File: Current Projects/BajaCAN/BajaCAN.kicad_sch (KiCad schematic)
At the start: 21 parts, among them J1 Conn_01x04, J2 ICSP, J3 Conn_01x04, U1 AVR128DB32x-xPT, U3 MCP1603, U4 MCP251863T-H-SS, Y1 OV-7604-C7, Y2 CSTNE16M0VH3C000R0

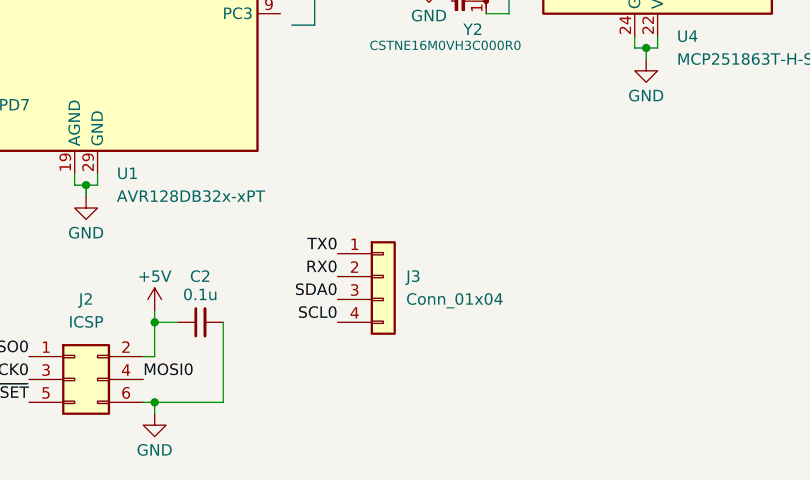
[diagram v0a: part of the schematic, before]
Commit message: Deleted extra header
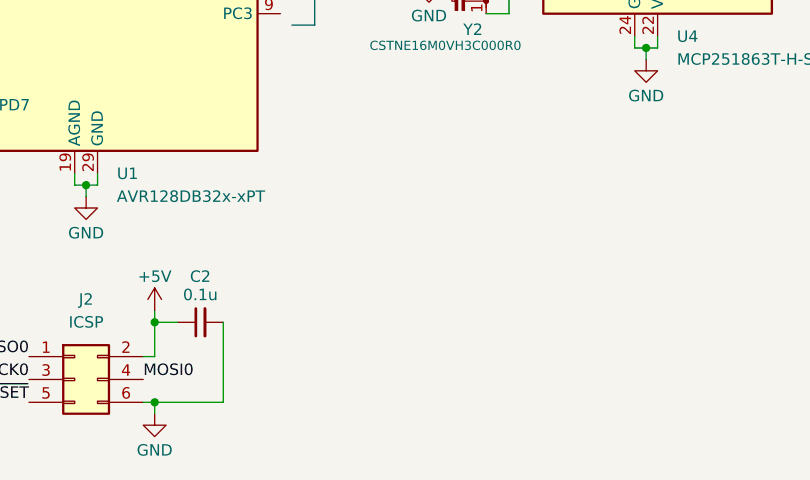
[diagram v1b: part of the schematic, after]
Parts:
- removed J3: Conn_01x04, symbol Connector_Generic:Conn_01x04
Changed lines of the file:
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@@
-	)
-	(label "RX0"
-		(at 172.72 134.62 180)
-		(effects
-			(font
-				(size 1.27 1.27)
-			)
-			(justify right bottom)
-		)
 	)
 	(label "RX0"
@@
 		)
 	)
-	(label "SCL0"
-		(at 172.72 139.7 180)
-		(effects
-			(font
-				(size 1.27 1.27)
-			)
-			(justify right bottom)
-		)
-	)
 	(label "CAN_L"
 		(at 245.11 74.93 180)
@@
 		)
 	)
-	(label "SDA0"
-		(at 172.72 137.16 180)
-		(effects
-			(font
-				(size 1.27 1.27)
-			)
-			(justify right bottom)
-		)
-	)
 	(label "SCK0"
 		(at 138.43 146.05 180)
@@
 	(label "~{RESET}"
 		(at 138.43 148.59 180)
-		(effects
-			(font
-				(size 1.27 1.27)
-			)
-			(justify right bottom)
-		)
-	)
-	(label "TX0"
-		(at 172.72 132.08 180)
 		(effects
 			(font
@@
 					(unit 1)
 				)
-			)
-		)
-	)
-	(symbol
-		(lib_id "Connector_Generic:Conn_01x04")
-		(at 177.8 134.62 0)
-		(unit 1)
-		(exclude_from_sim no)
-		(in_bom yes)
-		(on_board yes)
-		(dnp no)
-		(fields_autoplaced yes)
-		(property "Reference" "J3"
-			(at 180.34 134.6199 0)
-			(effects
-				(font
-					(size 1.27 1.27)
-				)
-				(justify left)
-			)
-		)
-		(property "Value" "Conn_01x04"
-			(at 180.34 137.1599 0)
-			(effects
-				(font
-					(size 1.27 1.27)
-				)
-				(justify left)
-			)
-		)
-		(property "Footprint" ""
-			(at 177.8 134.62 0)
-			(effects
-				(font
-					(size 1.27 1.27)
-				)
-				(hide yes)
-			)
-		)
-		(property "Datasheet" "~"
-			(at 177.8 134.62 0)
-			(effects
-				(font
-					(size 1.27 1.27)
-				)
-				(hide yes)
-			)
-		)
-		(property "Description" "Generic connector, single row, 01x04, script generated (kicad-library-utils/schlib/autogen/connector/)"
-			(at 177.8 134.62 0)
-			(effects
-				(font
-					(size 1.27 1.27)
-				)
-				(hide yes)
-			)
-		)
-		(pin "1"
-		)
-		(pin "2"
-		)
-		(pin "3"
-		)
-		(pin "4"
-		)
-		(instances
-			(project ""
-				(path "/e8fd5210-53c5-4e8b-9e8d-a6cec89a0b03"
-					(reference "J3")
-					(unit 1)
-				)

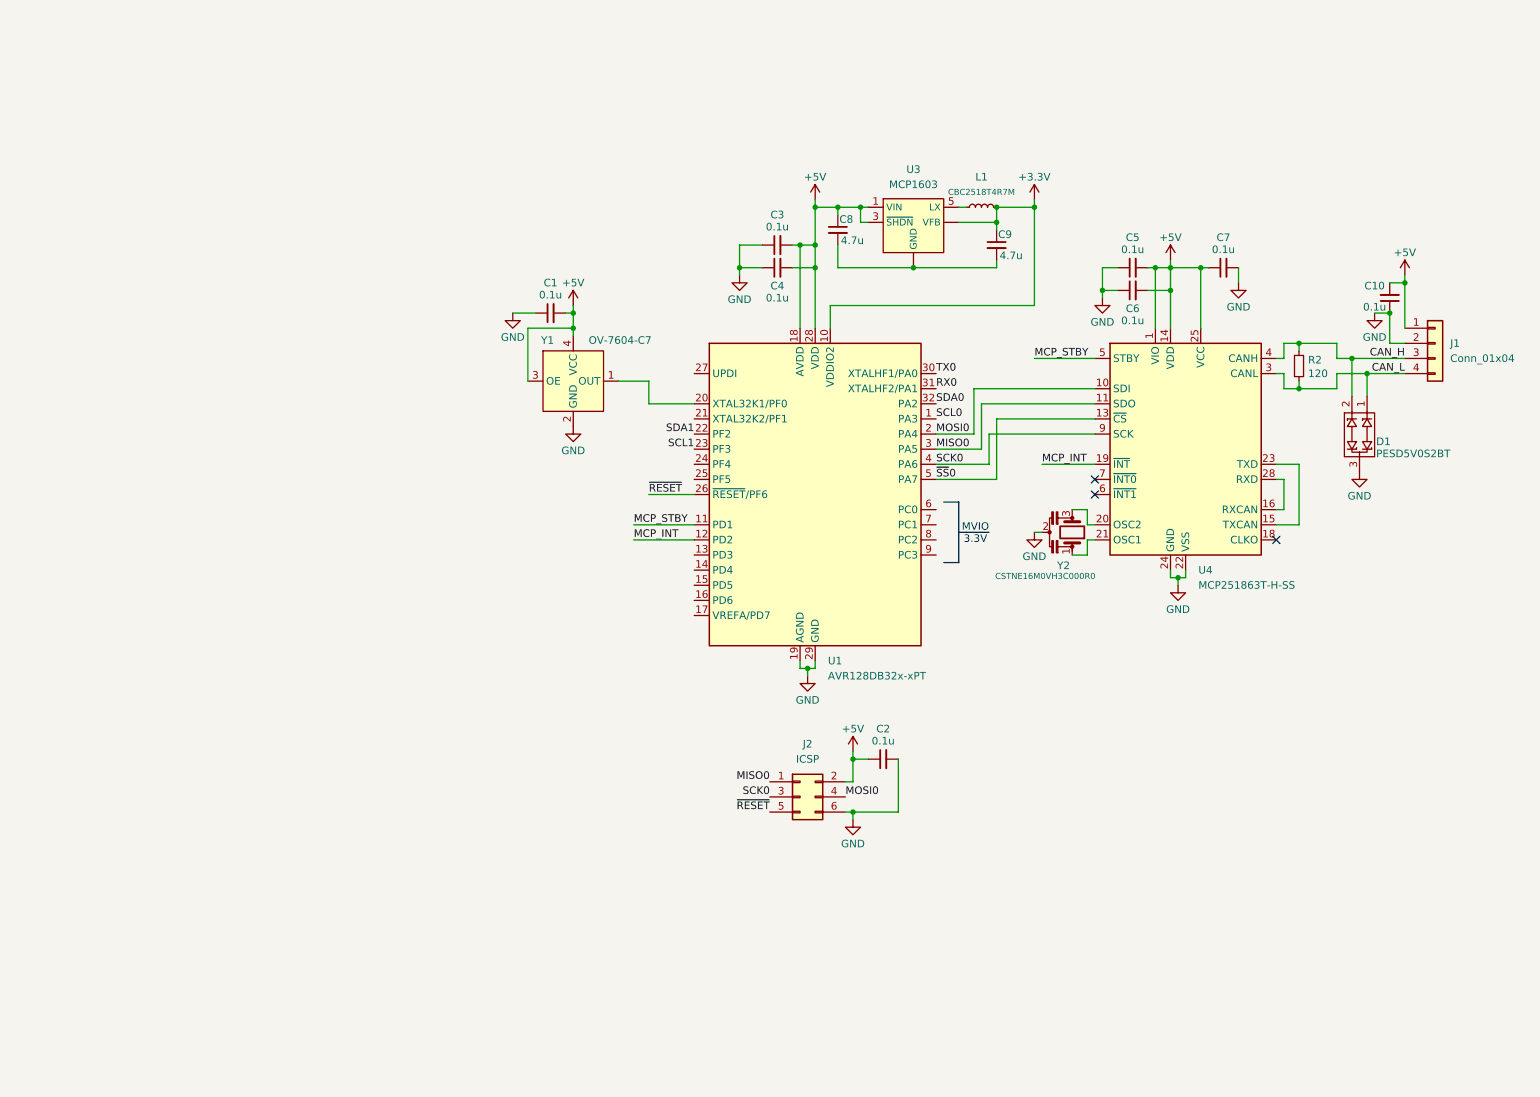
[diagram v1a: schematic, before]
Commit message: Added I/O molex conns
A and D keyed
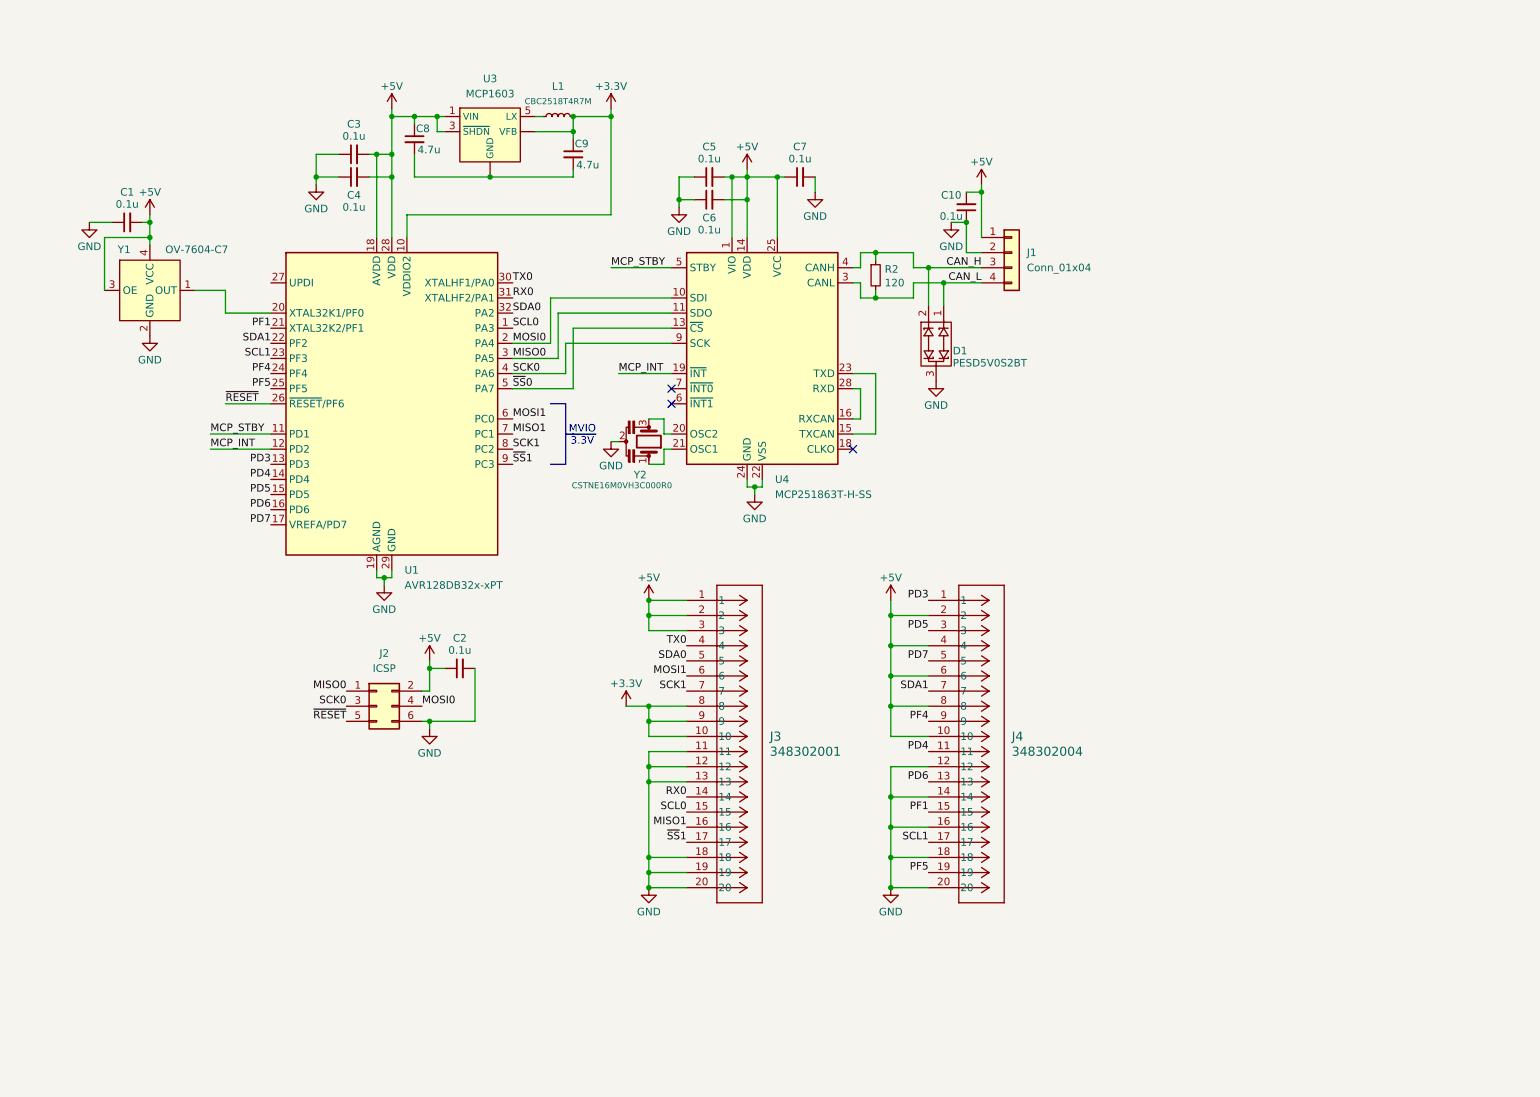
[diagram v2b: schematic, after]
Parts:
- added J3: 348302001, molex:CONN_SD-34829-001_20_ST_MOL, symbol molex:348302001
- added J4: 348302004, molex:CONN_SD-34829-001_20_ST_MOL, symbol molex:348302004
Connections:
- net +3.3V: now also J3.10, J3.8, J3.9
- net +5V: now also J3.1, J3.2, J3.3, J4.10, J4.2, J4.4, J4.6, J4.8
- net GND: now also J3.11, J3.12, J3.13, J3.18, J3.19, J3.20, J4.12, J4.14, J4.16, J4.18, J4.20
- net RX0: now also J3.14
- net SCL0: now also J3.15
- net SCL1: now also J4.17
- net SDA0: now also J3.5
- net SDA1: now also J4.7
- net TX0: now also J3.4
- net PD3: now reaches U1.13 (PD3)
- net PD3: now also J4.1
- net PD4: now reaches U1.14 (PD4)
- net PD4: now also J4.11
- net PD5: now reaches U1.15 (PD5)
- net PD5: now also J4.3
- net PD6: now reaches U1.16 (PD6)
- net PD6: now also J4.13
- net PD7: now reaches U1.17 (VREFA/PD7)
- net PD7: now also J4.5
- net PF1: now reaches U1.21 (XTAL32K2/PF1)
- net PF1: now also J4.15
- net PF4: now reaches U1.24 (PF4)
- net PF4: now also J4.9
- net PF5: now reaches U1.25 (PF5)
- net PF5: now also J4.19
- net MOSI1: now reaches U1.6 (PC0)
- net MOSI1: now also J3.6
- net MISO1: now reaches U1.7 (PC1)
- net MISO1: now also J3.16
- net SCK1: now reaches U1.8 (PC2)
- net SCK1: now also J3.7
- net ~{SS}1: now reaches U1.9 (PC3)
- net ~{SS}1: now also J3.17
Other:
- company: (none) -> NCSU Baja
- title: (none) -> NCSU Baja CAN Node
- moved on the sheet: C1, C10, C2, C3, C4, C5, C6, C7, C8, C9, D1, J1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

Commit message: CAN Node layout and routing!
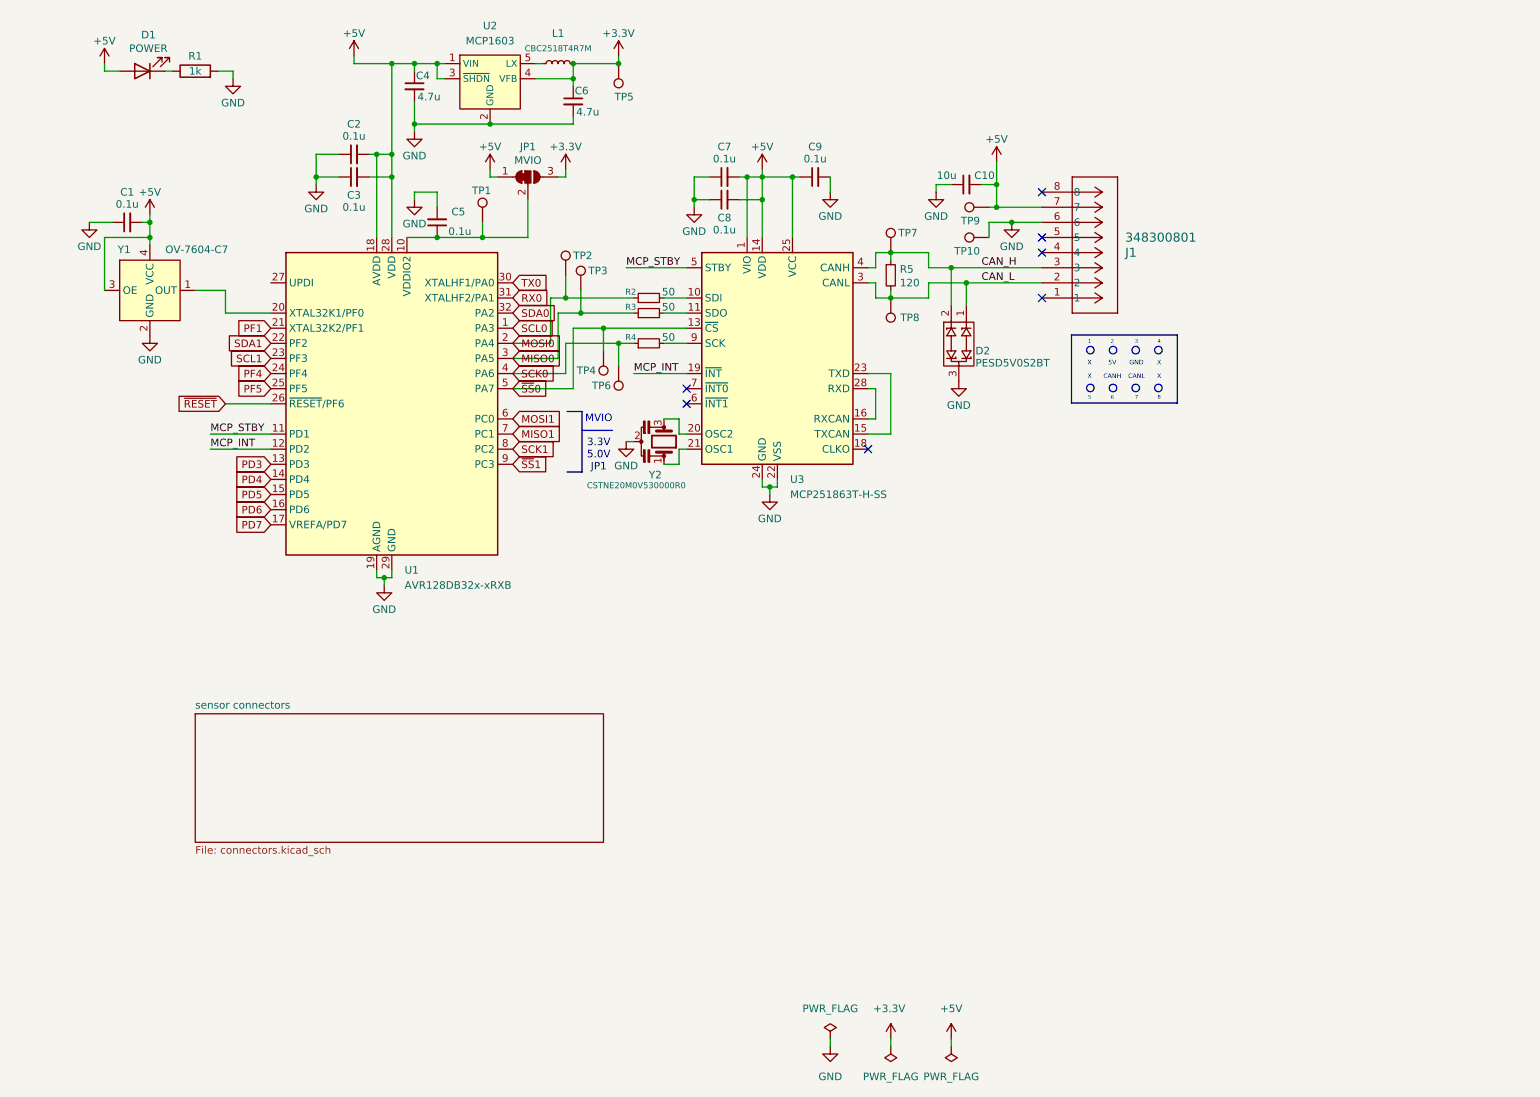
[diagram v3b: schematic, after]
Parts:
- removed C2: 0.1u, symbol Device:C_Small
- removed J1: Conn_01x04, symbol Connector_Generic:Conn_01x04
- removed J2: ICSP, symbol Connector_Generic:Conn_02x03_Odd_Even
- removed J3: 348302001, molex:CONN_SD-34829-001_20_ST_MOL, symbol molex:348302001
- removed J4: 348302004, molex:CONN_SD-34829-001_20_ST_MOL, symbol molex:348302004
- added C5: 0.1u, Capacitor_SMD:C_0603_1608Metric, symbol Device:C_Small
- added D1: POWER, LED_SMD:LED_0805_2012Metric, symbol Device:LED
- added J1: 348300801, molex:CONN_SD-34829-001_08_ST_MOL, symbol molex:348300801
- added JP1: MVIO, Jumper:SolderJumper-3_P1.3mm_Bridged12_RoundedPad1.0x1.5mm, symbol Jumper:SolderJumper_3_Bridged12
- added R1: 1k, Resistor_SMD:R_0603_1608Metric, symbol Device:R
- added R2, R3, R4: 50, Resistor_SMD:R_0603_1608Metric, symbol Device:R_Small
- added TP1: TestPoint, TestPoint:TestPoint_Pad_D1.5mm, symbol Connector:TestPoint
- added TP10, TP5, TP9: TestPoint, TestPoint:TestPoint_Pad_D2.0mm, symbol Connector:TestPoint
- added TP2, TP3, TP4, TP6, TP7, TP8: TestPoint, TestPoint:TestPoint_Pad_D1.0mm, symbol Connector:TestPoint
- C1: footprint (none) -> Capacitor_SMD:C_0603_1608Metric
- C10: value 0.1u -> 10u; footprint (none) -> Capacitor_SMD:C_Elec_4x5.4
- C2: renamed from C3; footprint (none) -> Capacitor_SMD:C_0603_1608Metric
- C3: renamed from C4; footprint (none) -> Capacitor_SMD:C_0603_1608Metric
- C4: renamed from C8; footprint (none) -> Capacitor_SMD:C_0805_2012Metric
- C6: renamed from C9; footprint (none) -> Capacitor_SMD:C_0805_2012Metric
- C7: renamed from C5; footprint (none) -> Capacitor_SMD:C_0603_1608Metric
- C8: renamed from C6; footprint (none) -> Capacitor_SMD:C_0603_1608Metric
- C9: renamed from C7; footprint (none) -> Capacitor_SMD:C_0603_1608Metric
- L1: footprint (none) -> Inductor_SMD:L_1008_2520Metric
- R5: renamed from R2; footprint (none) -> Resistor_SMD:R_0603_1608Metric
- U1: value AVR128DB32x-xPT -> AVR128DB32x-xRXB; footprint Package_QFP:TQFP-32_7x7mm_P0.8mm -> Package_DFN_QFN:QFN-32-1EP_5x5mm_P0.5mm_EP3.1x3.1mm; symbol MCU_Microchip_AVR_Dx:AVR128DB32x-xPT -> MCU_Microchip_AVR_Dx:AVR128DB32x-xRXB
- U2: renamed from U3; footprint Package_TO_SOT_SMD:TSOT-23-5_HandSoldering -> Package_TO_SOT_SMD:TSOT-23-5
- Y1: footprint oscillator:OV-7604-C7 -> oscillator:OSC_OV-7604-C7-32.768KHZ-20PPM-TA-QC
- Y2: value CSTNE16M0VH3C000R0 -> CSTNE20M0V530000R0; footprint Crystal:Resonator_SMD_Murata_CSTxExxV-3Pin_3.0x1.1mm_HandSoldering -> Crystal:Resonator_SMD_Murata_CSTxExxV-3Pin_3.0x1.1mm
- renumbered D1 to D2, U4 to U3
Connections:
- net +3.3V: now also U2.4 (VFB), JP1.3 (B), TP5.1; no longer U1.10 (VDDIO2), U2. (VFB)
- net +5V: now also D1.2 (A), J1.7, JP1.1 (A), TP9.1
- net CAN_H: now also J1.3, TP7.1
- net CAN_L: now also J1.2, TP8.1
- net GND: now also C4.2, C6.2, U1.33 (GND), U2.2 (GND), C5.2, J1.6, R1.2, TP10.1
- net MISO0: now also R3.1, TP3.1; no longer U3.11 (SDO)
- net MOSI0: now also R2.1, TP2.1; no longer U3.10 (SDI)
- net SCK0: now also R4.1, TP6.1; no longer U3.9 (SCK)
- net ~{SS}0: now also TP4.1
- new net: R2.2, U3.10 (SDI)
- new net: C5.1, JP1.2 (C), TP1.1, U1.10 (VDDIO2)
- new net: R3.2, U3.11 (SDO)
- new net: R4.2, U3.9 (SCK)
- new net: D1.1 (K), R1.1
- no-connect marks 3 -> 7
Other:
- added sheet sensor connectors (connectors.kicad_sch)
- note added: "1"
- note added: "2"
- note added: "3"
- note added: "3.3V 5.0V JP1"
- note added: "4"
- note added: "5"
- note added: "5V"
- note added: "6"
- note added: "7"
- note added: "8"
- note added: "CANH"
- note added: "CANL"
- note added: "GND"
- note added: "X"
- note removed: "3.3V"
- moved on the sheet: C10, C4, C6, C7, C8, C9, D2, L1, R5, U3, Y2
